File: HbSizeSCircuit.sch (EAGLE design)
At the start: 20 parts

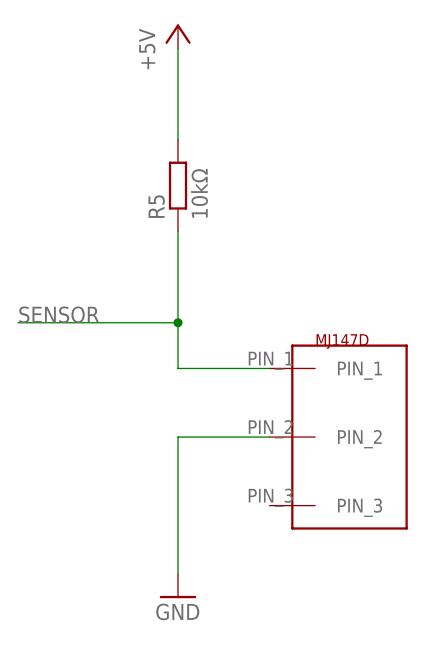
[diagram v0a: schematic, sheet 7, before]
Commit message: add board layout
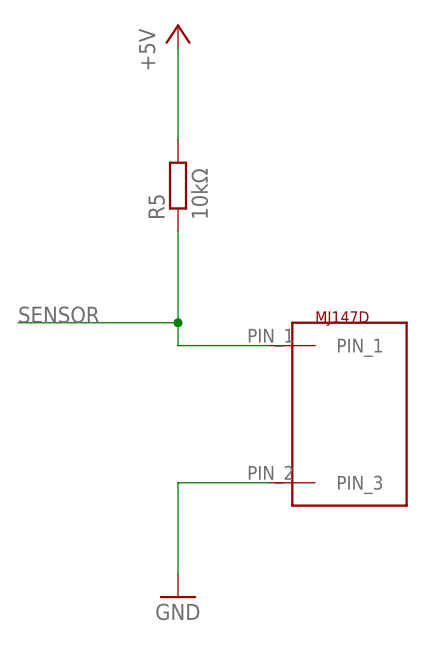
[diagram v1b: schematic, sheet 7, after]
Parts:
- U$10: value MJ147D -> MJ147D_2PIN; device HbHandBoard_SizeS:MJ147D -> HbHandBoard_SizeS:MJ147D_2PIN
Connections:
- net GND: now also U$10.PIN_3; no longer U$10.PIN_2
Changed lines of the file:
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@@
 <part name="R3" library="resistor" library_urn="urn:adsk.eagle:library:348" deviceset="R-EU_" device="M1206" package3d_urn="urn:adsk.eagle:package:26088/1" value="200Ω"/>
 <part name="U$6" library="HbHandBoard_SizeS" deviceset="POLOLU_A_STAR_32U4_MICRO_SMD" device=""/>
-<part name="U$10" library="HbHandBoard_SizeS" deviceset="MJ147D" device=""/>
 <part name="P+6" library="supply1" library_urn="urn:adsk.eagle:library:371" deviceset="+5V" device=""/>
 <part name="GND7" library="supply1" library_urn="urn:adsk.eagle:library:371" deviceset="GND" device=""/>
 <part name="R5" library="resistor" library_urn="urn:adsk.eagle:library:348" deviceset="R-EU_" device="R1206" package3d_urn="urn:adsk.eagle:package:26062/1" value="10kΩ"/>
+<part name="U$10" library="HbHandBoard_SizeS" deviceset="MJ147D_2PIN" device=""/>
 </parts>
 <sheets>
@@
 </plain>
 <instances>
-<instance part="U$10" gate="G$1" x="15.24" y="17.78"/>
 <instance part="P+6" gate="1" x="0" y="58.42"/>
 <instance part="GND7" gate="1" x="0" y="-5.08"/>
 <instance part="R5" gate="G$1" x="0" y="40.64" rot="R90"/>
+<instance part="U$10" gate="G$1" x="15.24" y="20.32"/>
 </instances>
 <busses>
@@
 <net name="SENSOR" class="0">
 <segment>
-<pinref part="U$10" gate="G$1" pin="PIN_1"/>
-<wire x1="10.16" y1="20.32" x2="0" y2="20.32" width="0.1524" layer="91"/>
+<wire x1="10.16" y1="22.86" x2="0" y2="22.86" width="0.1524" layer="91"/>
 <pinref part="R5" gate="G$1" pin="1"/>
 <wire x1="0" y1="35.56" x2="0" y2="25.4" width="0.1524" layer="91"/>
-<wire x1="0" y1="25.4" x2="0" y2="20.32" width="0.1524" layer="91"/>
+<wire x1="0" y1="25.4" x2="0" y2="22.86" width="0.1524" layer="91"/>
 <wire x1="0" y1="25.4" x2="-17.78" y2="25.4" width="0.1524" layer="91"/>
 <junction x="0" y="25.4"/>
 <label x="-17.78" y="25.4" size="1.778" layer="95"/>
+<pinref part="U$10" gate="G$1" pin="PIN_1"/>
 </segment>
 </net>
@@
 <segment>
 <pinref part="GND7" gate="1" pin="GND"/>
-<pinref part="U$10" gate="G$1" pin="PIN_2"/>
-<wire x1="0" y1="-2.54" x2="0" y2="12.7" width="0.1524" layer="91"/>
-<wire x1="0" y1="12.7" x2="10.16" y2="12.7" width="0.1524" layer="91"/>
-</segment>
-</net>
+<wire x1="0" y1="-2.54" x2="0" y2="7.62" width="0.1524" layer="91"/>
+<wire x1="0" y1="7.62" x2="10.16" y2="7.62" width="0.1524" layer="91"/>
+<pinref part="U$10" gate="G$1" pin="PIN_3"/>
+</segment>
+</net>

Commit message: 回路図を一枚にまとめた
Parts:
- removed 100KΩ: (no value), resistor:R-EU_M1206
- removed C1: 10uF, resistor:C-USC1206
- removed C2: 22uF, resistor:C-USC1206
- removed R1: 1kΩ, resistor:R-EU_M1206
- removed R2: 1.2kΩ, resistor:R-EU_M1206
- removed R3: 200Ω, resistor:R-EU_M1206
- removed R4: 10kΩ, resistor:R-EU_R1206
- removed U$4, U$5: SKRPACE010, HbHandBoard_SizeM:SKRPACE010
- removed U$7: HEC3110-01-010, HbHandBoard_SizeS:HEC3110-01-010
- removed U$8: OKL_T3_W12, HbHandBoard_SizeS:OKL_T3_W12
- added 100KΩ1: (no value), resistor:R-EU_M1206
- added C3: 10uF, resistor:C-USC1206
- added C4: 22uF, resistor:C-USC1206
- added R6, R8: 10kΩ, resistor:R-EU_R1206
- added R7: 1.2kΩ, resistor:R-EU_M1206
- added R9: 200Ω, resistor:R-EU_M1206
- added U$13: MJ147D_2PIN, HbHandBoard_SizeS:MJ147D_2PIN
- added U$14, U$15: 53398-0371, HbHandBoard_SizeS:53398-0371
- added U$16: SKRPACE010, HbHandBoard_SizeM:SKRPACE010
- R5: value 10kΩ -> 1kΩ; device resistor:R-EU_R1206 -> resistor:R-EU_M1206
- U$1: value SKRPACE010 -> OKL_T3_W12; device HbHandBoard_SizeM:SKRPACE010 -> HbHandBoard_SizeS:OKL_T3_W12
- U$10: value MJ147D_2PIN -> POLOLU_A_STAR_32U4_MICRO_SMD; device HbHandBoard_SizeS:MJ147D_2PIN -> HbHandBoard_SizeS:POLOLU_A_STAR_32U4_MICRO_SMD
- U$11, U$12, U$9: value 53398-0371 -> SKRPACE010; device HbHandBoard_SizeS:53398-0371 -> HbHandBoard_SizeM:SKRPACE010
- U$2: value IS-1250_POWERSWITCH -> HEC3110-01-010; device HbHandBoard_SizeS:IS-1250_POWERSWITCH -> HbHandBoard_SizeS:HEC3110-01-010
- U$3: value SKRPACE010 -> IS-1250_POWERSWITCH; device HbHandBoard_SizeM:SKRPACE010 -> HbHandBoard_SizeS:IS-1250_POWERSWITCH
- U$6: value POLOLU_A_STAR_32U4_MICRO_SMD -> 53398-0371; device HbHandBoard_SizeS:POLOLU_A_STAR_32U4_MICRO_SMD -> HbHandBoard_SizeS:53398-0371
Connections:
- removed net N$1: R1.2, U$8.TRIM
- removed net N$2: R1.1, R3.2
- new net N$3: R5.2, U$1.TRIM
- new net N$4: C3.2, R7.1
- new net N$5: R5.1, R9.2
- net +5V: now also 100KΩ1.2, C3.1, R6.2, R7.2, U$1.SENSE, U$1.VOUT, U$10.VIN, U$14.VIN, U$15.VIN; no longer 100KΩ.2, C1.1, R2.2, R5.2, U$11.VIN, U$12.VIN, U$8.SENSE, U$8.VOUT, U$9.VIN
- net GND: now also C4.2, R9.1, U$1.GND, U$10.GND, U$11.A_LEFT, U$12.A_LEFT, U$13.PIN_3, U$14.GND, U$15.GND, U$16.A_LEFT, U$2.P$2, U$3.P_M_L, U$9.A_LEFT; no longer C1.2, C2.2, R2.1, R3.1, U$1.A_LEFT, U$10.PIN_3, U$11.GND, U$12.GND, U$2.P_M_L, U$3.A_LEFT, U$4.A_LEFT, U$5.A_LEFT, U$7.P$2, U$8.GND, U$9.GND
- net PGOOD: now also 100KΩ1.1, U$1.PGOOD, U$10.GPIO_8; no longer 100KΩ.1, U$6.GPIO_8, U$8.PGOOD
- net PIN_INDEXSERVO: now also U$10.GPIO_9, U$15.SIG; no longer U$12.SIG, U$6.GPIO_9
- net PIN_ON/OFF: now also R8.1, U$1.ON/OFF, U$3.P_U_L; no longer R4.1, U$2.P_U_L, U$8.ON/OFF
- net PIN_OTHERSERVO: now also U$10.GPIO_6, U$14.SIG; no longer U$11.SIG, U$6.GPIO_6
- net PIN_THUMBSERVO: now also U$10.GPIO_5, U$6.SIG; no longer U$6.GPIO_5, U$9.SIG
- net SENSOR: now also R6.1, U$10.A0, U$13.PIN_1; no longer R5.1, U$10.PIN_1, U$6.A0
- net SWITCH_HOLD: now also U$10.GPIO_0, U$16.B_RIGHT; no longer U$5.B_RIGHT, U$6.GPIO_0
- net SWITCH_INIT: now also U$10.GPIO_1, U$9.B_RIGHT; no longer U$1.B_RIGHT, U$6.GPIO_1
- net SWITCH_MODE: now also U$10.GPIO_2, U$11.B_RIGHT; no longer U$3.B_RIGHT, U$6.GPIO_2
- net SWITCH_THUMB: now also U$10.GPIO_3, U$12.B_RIGHT; no longer U$4.B_RIGHT, U$6.GPIO_3
- net V+: now also C4.1, R8.2, U$1.VIN, U$2.P$1; no longer C2.1, R4.2, U$7.P$1, U$8.VIN
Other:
- note added: "1.0"
- note added: "<descriptive text>"
- note added: "<name>"
- note added: "A3"
- note added: "Aproved:"
- note added: "Checked:"
- note added: "DC Jack Block"
- note added: "DCDC Converter Block"
- note added: "Date:"
- note added: "Description:"
- note added: "Engineer:"
- note added: "Filename:"
- note added: "Koki Shinjo"
- note added: "MAJ"
- note added: "MicroController Block"
- note added: "Page:"
- note added: "Power Switch Block"
- note added: "Revision:"
- note added: "Sensor Block"
- note added: "Servo Connector Block"
- note added: "Size:"
- note added: "Tact Switch Block"
